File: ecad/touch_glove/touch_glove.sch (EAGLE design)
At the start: 374 parts, among them IC1 DRV8662, J1 VERT MALE 2.54MM, J2 VERT MALE 2.54MM, J3 VERT MALE 2.54MM, J4 VERT MALE 2.54MM, J5 VERT MALE 2.54MM, J6 PTH VERT MALE, J7 PTH VERT MALE, J8 PTH VERT MALE, J9 PTH VERT MALE, Q1 MCH3474 4A/30V, Q2 MCH3474 4A/30V, Q3 MCH3474 4A/30V, Q4 MCH3474 4A/30V, Q5 MCH3474 4A/30V, Q6 MCH3474 4A/30V, SW1 4A/28V, SW2 25mA/24V

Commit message: Create mcu to unity example code.  Create schematics for master thesis.  Edit robotic arm and touch glove pcb.
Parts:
- removed JP2: JUMPER_SMD_2-PAD_NO_SILK, _connectors:JUMPER_SMD_2-PAD_NO_SILK
- AVR_ISP: value PTH VERT MALE -> AVR ISP
- FTDI: value FTDI -> PTH RA VERT MALE; device _connectors:FTDI_PTH_RA-MALE -> _connectors:FTDI_PTH_RA_MALE_2.54MM
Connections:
- removed net AREF: JP2.2, MCU.AREF
- net A1.8V: now also MCU.AREF
- net VSENSOR: no longer JP2.1
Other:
- moved on the sheet: FTDI
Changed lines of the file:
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@@
 <setting verticaltext="up"/>
 </settings>
-<grid distance="0.1" unitdist="inch" unit="inch" style="lines" multiple="1" display="yes" altdistance="0.01" altunitdist="inch" altunit="inch"/>
+<grid distance="0.1" unitdist="inch" unit="inch" style="lines" multiple="1" display="no" altdistance="0.01" altunitdist="inch" altunit="inch"/>
 <layers>
 <layer number="1" name="Top" color="4" fill="1" visible="no" active="no"/>
@@
 <part name="GND125" library="_power_symbols" deviceset="GND" device=""/>
 <part name="SUPPLY84" library="_power_symbols" deviceset="VCC" device=""/>
-<part name="AVR_ISP" library="_connectors" deviceset="AVR_SPI_PRG_6" device="_PTH_VERT_MALE_2.54MM" package3d_urn="urn:adsk.eagle:package:4860635/1" value="PTH VERT MALE"/>
+<part name="AVR_ISP" library="_connectors" deviceset="AVR_SPI_PRG_6" device="_PTH_VERT_MALE_2.54MM" package3d_urn="urn:adsk.eagle:package:8712796/1" value="AVR ISP"/>
 <part name="C22" library="_capacitors" deviceset="0.1UF" device="_SMD-0402_50V-10%" package3d_urn="urn:adsk.eagle:package:2886515/1" value="0.1uF/50V"/>
-<part name="FTDI" library="_connectors" deviceset="FTDI" device="_PTH_RA-MALE" package3d_urn="urn:adsk.eagle:package:2993075/7" value="FTDI"/>
+<part name="FTDI" library="_connectors" deviceset="FTDI" device="_PTH_RA_MALE_2.54MM" package3d_urn="urn:adsk.eagle:package:8712641/1" value="PTH RA VERT MALE"/>
 <part name="GND127" library="_power_symbols" deviceset="GND" device=""/>
 <part name="GND128" library="_power_symbols" deviceset="GND" device=""/>
@@
 <part name="SUPPLY3" library="_power_symbols" deviceset="NGND" device=""/>
 <part name="SUPPLY6" library="_power_symbols" deviceset="NGND" device=""/>
-<part name="SW1" library="_switches" library_urn="urn:adsk.eagle:library:8465428" deviceset="SWITCH_SPDT" device="_RA_PTH_4A-28V_L12.7-W9.5" package3d_urn="urn:adsk.eagle:package:2973750/5" value="4A/28V"/>
+<part name="SW1" library="_switches" deviceset="SWITCH_SPDT" device="_RA_PTH_4A-28V_L12.7-W9.5" package3d_urn="urn:adsk.eagle:package:2973750/2" value="4A/28V"/>
 <part name="C1" library="_capacitors" deviceset="100UF-POLARIZED" device="_TANT_SMD-1206_10V-20%" package3d_urn="urn:adsk.eagle:package:6906990/1" value="100uF/10V"/>
 <part name="SUPPLY4" library="_power_symbols" deviceset="GND" device=""/>
@@
 <part name="SUPPLY120" library="_power_symbols" deviceset="VSENSOR" device=""/>
 <part name="SUPPLY121" library="_power_symbols" deviceset="VSENSOR" device=""/>
-<part name="JP2" library="_connectors" deviceset="JUMPER_SMD_2-PAD_NO" device="_SILK"/>
-<part name="SUPPLY13" library="_power_symbols" deviceset="VSENSOR" device=""/>
 <part name="SUPPLY15" library="_power_symbols" deviceset="VBAT" device=""/>
 <part name="OPAMP1" library="_op_amps" deviceset="LM358" device="_DFN-EP" package3d_urn="urn:adsk.eagle:package:2992818/3" value="LM358"/>
@@
 <part name="J9" library="_connectors" deviceset="1X02" device="_PTH_VERT_MALE_2.54MM" package3d_urn="urn:adsk.eagle:package:4781708/8" value="PTH VERT MALE"/>
 <part name="SUPPLY51" library="_power_symbols" deviceset="NGND" device=""/>
+<part name="SUPPLY52" library="_power_symbols" deviceset="A1.8V" device=""/>
 </parts>
 <sheets>
@@
 <instance part="SUPPLY120" gate="G$1" x="436.88" y="436.88" smashed="yes"/>
 <instance part="SUPPLY121" gate="G$1" x="447.04" y="436.88" smashed="yes"/>
-<instance part="JP2" gate="G$1" x="297.18" y="411.48" smashed="yes">
-<attribute name="NAME" x="297.18" y="413.258" size="1.27" layer="95" font="vector" ratio="10" align="bottom-center"/>
-</instance>
-<instance part="SUPPLY13" gate="G$1" x="289.56" y="419.1" smashed="yes"/>
 <instance part="SUPPLY15" gate="G$1" x="274.32" y="274.32" smashed="yes"/>
 <instance part="OPAMP1" gate="G$1" x="548.64" y="330.2" smashed="yes">
@@
 </instance>
 <instance part="SUPPLY51" gate="G$1" x="662.94" y="454.66" smashed="yes"/>
+<instance part="SUPPLY52" gate="G$1" x="299.72" y="419.1" smashed="yes"/>
 </instances>
 <busses>
@@
 <segment>
 <pinref part="FTDI" gate="G$1" pin="GND"/>
-<wire x1="246.38" y1="91.44" x2="248.92" y2="91.44" width="0.1524" layer="91"/>
+<wire x1="243.84" y1="91.44" x2="248.92" y2="91.44" width="0.1524" layer="91"/>
 <wire x1="248.92" y1="91.44" x2="248.92" y2="88.9" width="0.1524" layer="91"/>
 <pinref part="GND127" gate="GND" pin="GND"/>
@@
 <segment>
 <pinref part="FTDI" gate="G$1" pin="TXO"/>
-<wire x1="251.46" y1="96.52" x2="246.38" y2="96.52" width="0.1524" layer="91"/>
+<wire x1="251.46" y1="96.52" x2="243.84" y2="96.52" width="0.1524" layer="91"/>
 <label x="251.46" y="96.52" size="1.27" layer="95" font="vector" ratio="10" xref="yes"/>
 </segment>
@@
 <segment>
 <pinref part="FTDI" gate="G$1" pin="RXI"/>
-<wire x1="246.38" y1="99.06" x2="251.46" y2="99.06" width="0.1524" layer="91"/>
+<wire x1="243.84" y1="99.06" x2="251.46" y2="99.06" width="0.1524" layer="91"/>
 <label x="251.46" y="99.06" size="1.27" layer="95" font="vector" ratio="10" xref="yes"/>
 </segment>
@@
 <pinref part="FTDI" gate="G$1" pin="DTR"/>
 <pinref part="C22" gate="G$1" pin="1"/>
-<wire x1="259.08" y1="101.6" x2="246.38" y2="101.6" width="0.1524" layer="91"/>
+<wire x1="259.08" y1="101.6" x2="243.84" y2="101.6" width="0.1524" layer="91"/>
 </segment>
 </net>
@@
 </segment>
 <segment>
-<pinref part="SUPPLY13" gate="G$1" pin="VSENSOR"/>
-<wire x1="289.56" y1="419.1" x2="289.56" y2="411.48" width="0.1524" layer="91" style="longdash"/>
-<pinref part="JP2" gate="G$1" pin="1"/>
-<wire x1="289.56" y1="411.48" x2="292.1" y2="411.48" width="0.1524" layer="91" style="longdash"/>
-</segment>
-<segment>
 <pinref part="OPAMP1" gate="G$1" pin="V+"/>
 <wire x1="548.64" y1="345.44" x2="548.64" y2="342.9" width="0.1524" layer="91"/>
@@
 </segment>
 </net>
-<net name="AREF" class="0">
-<segment>
-<pinref part="JP2" gate="G$1" pin="2"/>
-<pinref part="MCU" gate="G$1" pin="AREF"/>
-<wire x1="302.26" y1="411.48" x2="304.8" y2="411.48" width="0.1524" layer="91" style="longdash"/>
-</segment>
-</net>
 <net name="S1" class="0">
 <segment>
@@
 <wire x1="279.4" y1="190.5" x2="279.4" y2="187.96" width="0.1524" layer="91"/>
 </segment>
+<segment>
+<pinref part="MCU" gate="G$1" pin="AREF"/>
+<wire x1="299.72" y1="411.48" x2="304.8" y2="411.48" width="0.1524" layer="91" style="longdash"/>
+<wire x1="299.72" y1="411.48" x2="299.72" y2="419.1" width="0.1524" layer="91"/>
+<pinref part="SUPPLY52" gate="G$1" pin="A1.8V"/>
+</segment>
 </net>
 <net name="INDEX_IN1-4" class="0">
@@
 </drawing>
 <compatibility>
-<note version="8.2" severity="warning">
-Since Version 8.2, EAGLE supports online libraries. The ids
-of those online libraries will not be understood (or retained)
-with this version.
+<note version="6.3" minversion="6.2.2" severity="warning">
+Since Version 6.2.2 text objects can contain more than one line,
+which will not be processed correctly with this version.
 </note>
 <note version="8.3" severity="warning">

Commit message: Create PCA9685Servo library.  Touch up Touch Glove PCB.  Major work completed on ET Extension.
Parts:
- removed C16, C19, C37, C49, C63, C64, C66, C67, C68, C69, C70, C76, C78, C80: 0.1uF/50V, _capacitors:0.1UF_SMD-0402_50V-10%
- removed C17, C20, C71, C72, C73, C75, C77, C79: 10uF/6.3V, _capacitors:10UF_CER_SMD-0402_6.3V-20%
- removed C61: 0.1uF/25V, _capacitors:0.1UF_SMD-0603_50V-20%
- removed C62: 0.1uF/250V, _capacitors:0.1UF_SMD-0805_250V-10%
- removed C65: 100uF/10V, _capacitors:100UF-POLARIZED_TANT_SMD-1206_10V-20%
- removed C74: 4.7uF/10V/0402, _capacitors:4.7UF_CER_SMD-0402_10V-20%
- removed ET_INDEX_PIXEL1-1, ET_INDEX_PIXEL1-10, ET_INDEX_PIXEL1-11, ET_INDEX_PIXEL1-12, ET_INDEX_PIXEL1-13, ET_INDEX_PIXEL1-14, ET_INDEX_PIXEL1-15, ET_INDEX_PIXEL1-16, ET_INDEX_PIXEL1-17, ET_INDEX_PIXEL1-18, ET_INDEX_PIXEL1-19, ET_INDEX_PIXEL1-2, ET_INDEX_PIXEL1-20, ET_INDEX_PIXEL1-3, ET_INDEX_PIXEL1-4, ET_INDEX_PIXEL1-5, ET_INDEX_PIXEL1-6, ET_INDEX_PIXEL1-7, ET_INDEX_PIXEL1-8, ET_INDEX_PIXEL1-9, ET_INDEX_PIXEL2-1, ET_INDEX_PIXEL2-10, ET_INDEX_PIXEL2-11, ET_INDEX_PIXEL2-12, ET_INDEX_PIXEL2-13, ET_INDEX_PIXEL2-14, ET_INDEX_PIXEL2-15, ET_INDEX_PIXEL2-16, ET_INDEX_PIXEL2-17, ET_INDEX_PIXEL2-18, ET_INDEX_PIXEL2-19, ET_INDEX_PIXEL2-2, ET_INDEX_PIXEL2-20, ET_INDEX_PIXEL2-3, ET_INDEX_PIXEL2-4, ET_INDEX_PIXEL2-5, ET_INDEX_PIXEL2-6, ET_INDEX_PIXEL2-7, ET_INDEX_PIXEL2-8, ET_INDEX_PIXEL2-9, ET_INDEX_PIXEL3-1, ET_INDEX_PIXEL3-10, ET_INDEX_PIXEL3-11, ET_INDEX_PIXEL3-12, ET_INDEX_PIXEL3-13, ET_INDEX_PIXEL3-14, ET_INDEX_PIXEL3-15, ET_INDEX_PIXEL3-16, ET_INDEX_PIXEL3-17, ET_INDEX_PIXEL3-18, ET_INDEX_PIXEL3-19, ET_INDEX_PIXEL3-2, ET_INDEX_PIXEL3-20, ET_INDEX_PIXEL3-3, ET_INDEX_PIXEL3-4, ET_INDEX_PIXEL3-5, ET_INDEX_PIXEL3-6, ET_INDEX_PIXEL3-7, ET_INDEX_PIXEL3-8, ET_INDEX_PIXEL3-9, ET_INDEX_PIXEL4-1, ET_INDEX_PIXEL4-10, ET_INDEX_PIXEL4-11, ET_INDEX_PIXEL4-12, ET_INDEX_PIXEL4-13, ET_INDEX_PIXEL4-14, ET_INDEX_PIXEL4-15, ET_INDEX_PIXEL4-16, ET_INDEX_PIXEL4-17, ET_INDEX_PIXEL4-18, ET_INDEX_PIXEL4-19, ET_INDEX_PIXEL4-2, ET_INDEX_PIXEL4-20, ET_INDEX_PIXEL4-3, ET_INDEX_PIXEL4-4, ET_INDEX_PIXEL4-5, ET_INDEX_PIXEL4-6, ET_INDEX_PIXEL4-7, ET_INDEX_PIXEL4-8, ET_INDEX_PIXEL4-9: SPST-NO 170mA 250V, _relay:RELAY_SOLID-STATE_SSR_170MA_250V_SPST-NO
- removed IC1: DRV8662, _special:DRV8662_PIEZO_HAPTICS_DRIVER_QFN-20-EP
- removed J1, J2, J3, J4, J5: VERT MALE 2.54MM, _connectors:1X16_PTH_VERT_MALE_2.54MM
- removed L3: 4.7uH/1.4A, _inductors:4.7UH_SMD-2520_1.4A-0.216OHM-20%
- removed L4: 10uH/380mA, _inductors:10UH_SMD-0603_0.38A-0.468OHM-10%
- removed NFET1: 2N7002DW, _transistors:MOSFET_N-CHANNEL_2-ARRAY_2N7002DW_115MA-60V
- removed OPAMP4: TLV2361_GP_20MA_7MHZ, _op_amps:TLV2361_GP_20MA_7MHZ
- removed POT1: 100K, _resistors:POTENTIOMETER_ST4ETB104_100K-1/4W-20%
- removed PWM_DRIVER2, PWM_DRIVER3, PWM_DRIVER4, PWM_DRIVER5, PWM_DRIVER6: PCA9685, _special:PCA9685_16-CH_12-BIT_PWM-DRIVER_TSSOP-28_PWM-DRIVER_16CH
- removed R100, R101, R102, R103, R104, R105, R106, R107, R108, R109, R110, R111, R112, R113, R114, R115, R116, R117, R118, R119, R120, R121, R122, R123, R124, R125, R126, R127, R128, R129, R130, R131, R132, R133, R134, R135, R49, R57, R58, R59, R60, R61, R62, R63, R64, R65, R66, R67, R68, R69, R70, R71, R72, R73, R74, R75, R76, R77, R78, R79, R80, R81, R82, R83, R84, R85, R86, R87, R88, R89, R90, R91, R92, R93, R94, R95, R96, R97, R98, R99: 1K, _resistors:1KΩ_SMD-0402_1/16W-5%
- removed R136, R137, R54, R55, R56: 10K, _resistors:10KΩ_SMD-0402_1/16W-5%
- removed R16, R17, R18, R19, R20, R21, R22, R23, R24, R25, R26, R27, R28, R29, R30, R31: 100, _resistors:100Ω_SMD-0402_1/16W-5%
- removed R50: 768K, _resistors:768KΩ_SMD-0402_1/16W-1%
- removed R51: 35.7K, _resistors:35.7KΩ_SMD-0402_1/16W-1%
- removed R52: 20K, _resistors:20KΩ_SMD-0402_1/16W-1%
- removed R53: 41.2K, _resistors:41.2KΩ_SMD-0402_1/16W-1%
- removed REXT: 7.5K, _resistors:7.5KΩ_SMD-0402_1/16W-1%
- removed SW2: 25mA/24V, _switches:SWITCH_SPST_ARRAY-3_SLIDE_DIP_SPST_25MA_24V
- removed VREG-MCU1: TPS76833QDR 1A/3.3V, _ic_power:VREG_TPS768XX_ULDO_FAST-TRANSIENT_TPS76833QDR_1A-3.3V
- removed VREG2: NCP1729 50mA, _ic_power:VREG_NCP1729_NEGATIVE_SWITCHED-CAP-INVERTER_50MA
- removed VREG3: TPS62202 300mA 1.8V, _ic_power:VREG_SWITCHING_TPS6220XTPS62202_300MA_1.8V
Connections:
- net AVCC renamed A3.3V
- removed net -1.8V: C72.1, OPAMP4.V-, VREG2.VOUT
- removed net C+: C71.1, VREG2.C+
- removed net C-: C71.2, VREG2.C-
- removed net EN: IC1.EN, R54.2, SW2.S3
- removed net FB: IC1.FB, R50.1, R51.2, R52.2, R53.2
- removed net GAIN0: IC1.GAIN0, NFET1.G2, R55.2, SW2.S2
- removed net GAIN1: IC1.GAIN1, NFET1.G1, R56.2, SW2.S1
- removed net IN+: C64.1, OPAMP4.OUT, POT1.CCW, POT1.S, R136.2
- removed net INDEX_IN1-1: ET_INDEX_PIXEL1-1.1, ET_INDEX_PIXEL1-13.1, ET_INDEX_PIXEL1-17.1, ET_INDEX_PIXEL1-5.1, ET_INDEX_PIXEL1-9.1, PWM_DRIVER2.PWM0, PWM_DRIVER3.PWM0, PWM_DRIVER4.PWM0, PWM_DRIVER5.PWM0, PWM_DRIVER6.PWM0
- removed net INDEX_IN1-2: ET_INDEX_PIXEL1-10.1, ET_INDEX_PIXEL1-14.1, ET_INDEX_PIXEL1-18.1, ET_INDEX_PIXEL1-2.1, ET_INDEX_PIXEL1-6.1, PWM_DRIVER2.PWM1, PWM_DRIVER3.PWM1, PWM_DRIVER4.PWM1, PWM_DRIVER5.PWM1, PWM_DRIVER6.PWM1
- removed net INDEX_IN1-3: ET_INDEX_PIXEL1-11.1, ET_INDEX_PIXEL1-15.1, ET_INDEX_PIXEL1-19.1, ET_INDEX_PIXEL1-3.1, ET_INDEX_PIXEL1-7.1, PWM_DRIVER2.PWM2, PWM_DRIVER3.PWM2, PWM_DRIVER4.PWM2, PWM_DRIVER5.PWM2, PWM_DRIVER6.PWM2
- removed net INDEX_IN1-4: ET_INDEX_PIXEL1-12.1, ET_INDEX_PIXEL1-16.1, ET_INDEX_PIXEL1-20.1, ET_INDEX_PIXEL1-4.1, ET_INDEX_PIXEL1-8.1, PWM_DRIVER2.PWM3, PWM_DRIVER3.PWM3, PWM_DRIVER4.PWM3, PWM_DRIVER5.PWM3, PWM_DRIVER6.PWM3
- removed net INDEX_IN2-1: ET_INDEX_PIXEL2-1.1, ET_INDEX_PIXEL2-11.1, ET_INDEX_PIXEL2-15.1, ET_INDEX_PIXEL2-19.1, ET_INDEX_PIXEL2-7.1, PWM_DRIVER2.PWM4, PWM_DRIVER3.PWM4, PWM_DRIVER4.PWM4, PWM_DRIVER5.PWM4, PWM_DRIVER6.PWM4
- removed net INDEX_IN2-2: ET_INDEX_PIXEL2-10.1, ET_INDEX_PIXEL2-14.1, ET_INDEX_PIXEL2-18.1, ET_INDEX_PIXEL2-2.1, ET_INDEX_PIXEL2-6.1, PWM_DRIVER2.PWM5, PWM_DRIVER3.PWM5, PWM_DRIVER4.PWM5, PWM_DRIVER5.PWM5, PWM_DRIVER6.PWM5
- removed net INDEX_IN2-3: ET_INDEX_PIXEL2-13.1, ET_INDEX_PIXEL2-17.1, ET_INDEX_PIXEL2-3.1, ET_INDEX_PIXEL2-5.1, ET_INDEX_PIXEL2-9.1, PWM_DRIVER2.PWM6, PWM_DRIVER3.PWM6, PWM_DRIVER4.PWM6, PWM_DRIVER5.PWM6, PWM_DRIVER6.PWM6
- removed net INDEX_IN2-4: ET_INDEX_PIXEL2-12.1, ET_INDEX_PIXEL2-16.1, ET_INDEX_PIXEL2-20.1, ET_INDEX_PIXEL2-4.1, ET_INDEX_PIXEL2-8.1, PWM_DRIVER2.PWM7, PWM_DRIVER3.PWM7, PWM_DRIVER4.PWM7, PWM_DRIVER5.PWM7, PWM_DRIVER6.PWM7
- removed net INDEX_IN3-1: ET_INDEX_PIXEL3-1.1, ET_INDEX_PIXEL3-13.1, ET_INDEX_PIXEL3-17.1, ET_INDEX_PIXEL3-5.1, ET_INDEX_PIXEL3-9.1, PWM_DRIVER2.PWM8, PWM_DRIVER3.PWM8, PWM_DRIVER4.PWM8, PWM_DRIVER5.PWM8, PWM_DRIVER6.PWM8
- removed net INDEX_IN3-2: ET_INDEX_PIXEL3-10.1, ET_INDEX_PIXEL3-14.1, ET_INDEX_PIXEL3-18.1, ET_INDEX_PIXEL3-2.1, ET_INDEX_PIXEL3-6.1, PWM_DRIVER2.PWM9, PWM_DRIVER3.PWM9, PWM_DRIVER4.PWM9, PWM_DRIVER5.PWM9, PWM_DRIVER6.PWM9
- removed net INDEX_IN3-3: ET_INDEX_PIXEL3-11.1, ET_INDEX_PIXEL3-15.1, ET_INDEX_PIXEL3-19.1, ET_INDEX_PIXEL3-3.1, ET_INDEX_PIXEL3-7.1, PWM_DRIVER2.PWM10, PWM_DRIVER3.PWM10, PWM_DRIVER4.PWM10, PWM_DRIVER5.PWM10, PWM_DRIVER6.PWM10
- removed net INDEX_IN3-4: ET_INDEX_PIXEL3-12.1, ET_INDEX_PIXEL3-16.1, ET_INDEX_PIXEL3-20.1, ET_INDEX_PIXEL3-4.1, ET_INDEX_PIXEL3-8.1, PWM_DRIVER2.PWM11, PWM_DRIVER3.PWM11, PWM_DRIVER4.PWM11, PWM_DRIVER5.PWM11, PWM_DRIVER6.PWM11
- removed net INDEX_IN4-1: ET_INDEX_PIXEL4-1.1, ET_INDEX_PIXEL4-13.1, ET_INDEX_PIXEL4-17.1, ET_INDEX_PIXEL4-5.1, ET_INDEX_PIXEL4-9.1, PWM_DRIVER2.PWM12, PWM_DRIVER3.PWM12, PWM_DRIVER4.PWM12, PWM_DRIVER5.PWM12, PWM_DRIVER6.PWM12
- removed net INDEX_IN4-2: ET_INDEX_PIXEL4-10.1, ET_INDEX_PIXEL4-14.1, ET_INDEX_PIXEL4-18.1, ET_INDEX_PIXEL4-2.1, ET_INDEX_PIXEL4-6.1, PWM_DRIVER2.PWM13, PWM_DRIVER3.PWM13, PWM_DRIVER4.PWM13, PWM_DRIVER5.PWM13, PWM_DRIVER6.PWM13
- removed net INDEX_IN4-3: ET_INDEX_PIXEL4-11.1, ET_INDEX_PIXEL4-15.1, ET_INDEX_PIXEL4-19.1, ET_INDEX_PIXEL4-3.1, ET_INDEX_PIXEL4-7.1, PWM_DRIVER2.PWM14, PWM_DRIVER3.PWM14, PWM_DRIVER4.PWM14, PWM_DRIVER5.PWM14, PWM_DRIVER6.PWM14
- removed net INDEX_IN4-4: ET_INDEX_PIXEL4-12.1, ET_INDEX_PIXEL4-16.1, ET_INDEX_PIXEL4-20.1, ET_INDEX_PIXEL4-4.1, ET_INDEX_PIXEL4-8.1, PWM_DRIVER2.PWM15, PWM_DRIVER3.PWM15, PWM_DRIVER4.PWM15, PWM_DRIVER5.PWM15, PWM_DRIVER6.PWM15
- removed net INDEX_OUT1-1: ET_INDEX_PIXEL1-1.3, ET_INDEX_PIXEL1-13.3, ET_INDEX_PIXEL1-17.3, ET_INDEX_PIXEL1-5.3, ET_INDEX_PIXEL1-9.3, J1.1, J2.1, J3.1, J4.1, J5.1
- removed net INDEX_OUT1-2: ET_INDEX_PIXEL1-10.3, ET_INDEX_PIXEL1-14.3, ET_INDEX_PIXEL1-18.3, ET_INDEX_PIXEL1-2.3, ET_INDEX_PIXEL1-6.3
- removed net INDEX_OUT1-3: ET_INDEX_PIXEL1-11.3, ET_INDEX_PIXEL1-15.3, ET_INDEX_PIXEL1-19.3, ET_INDEX_PIXEL1-3.3, ET_INDEX_PIXEL1-7.3
- removed net INDEX_OUT1-4: ET_INDEX_PIXEL1-12.3, ET_INDEX_PIXEL1-16.3, ET_INDEX_PIXEL1-20.3, ET_INDEX_PIXEL1-4.3, ET_INDEX_PIXEL1-8.3
- removed net INDEX_OUT2-1: ET_INDEX_PIXEL2-1.3, ET_INDEX_PIXEL2-11.3, ET_INDEX_PIXEL2-15.3, ET_INDEX_PIXEL2-19.3, ET_INDEX_PIXEL2-7.3
- removed net INDEX_OUT2-2: ET_INDEX_PIXEL2-10.3, ET_INDEX_PIXEL2-14.3, ET_INDEX_PIXEL2-18.3, ET_INDEX_PIXEL2-2.3, ET_INDEX_PIXEL2-6.3
- removed net INDEX_OUT2-3: ET_INDEX_PIXEL2-13.3, ET_INDEX_PIXEL2-17.3, ET_INDEX_PIXEL2-3.3, ET_INDEX_PIXEL2-5.3, ET_INDEX_PIXEL2-9.3
- removed net INDEX_OUT2-4: ET_INDEX_PIXEL2-12.3, ET_INDEX_PIXEL2-16.3, ET_INDEX_PIXEL2-20.3, ET_INDEX_PIXEL2-4.3, ET_INDEX_PIXEL2-8.3
- removed net INDEX_OUT3-1: ET_INDEX_PIXEL3-1.3, ET_INDEX_PIXEL3-13.3, ET_INDEX_PIXEL3-17.3, ET_INDEX_PIXEL3-5.3, ET_INDEX_PIXEL3-9.3
- removed net INDEX_OUT3-2: ET_INDEX_PIXEL3-10.3, ET_INDEX_PIXEL3-14.3, ET_INDEX_PIXEL3-18.3, ET_INDEX_PIXEL3-2.3, ET_INDEX_PIXEL3-6.3
- removed net INDEX_OUT3-3: ET_INDEX_PIXEL3-11.3, ET_INDEX_PIXEL3-15.3, ET_INDEX_PIXEL3-19.3, ET_INDEX_PIXEL3-3.3, ET_INDEX_PIXEL3-7.3
- removed net INDEX_OUT3-4: ET_INDEX_PIXEL3-12.3, ET_INDEX_PIXEL3-16.3, ET_INDEX_PIXEL3-20.3, ET_INDEX_PIXEL3-4.3, ET_INDEX_PIXEL3-8.3
- removed net INDEX_OUT4-1: ET_INDEX_PIXEL4-1.3, ET_INDEX_PIXEL4-13.3, ET_INDEX_PIXEL4-17.3, ET_INDEX_PIXEL4-5.3, ET_INDEX_PIXEL4-9.3
- removed net INDEX_OUT4-2: ET_INDEX_PIXEL4-10.3, ET_INDEX_PIXEL4-14.3, ET_INDEX_PIXEL4-18.3, ET_INDEX_PIXEL4-2.3, ET_INDEX_PIXEL4-6.3
- removed net INDEX_OUT4-3: ET_INDEX_PIXEL4-11.3, ET_INDEX_PIXEL4-15.3, ET_INDEX_PIXEL4-19.3, ET_INDEX_PIXEL4-3.3, ET_INDEX_PIXEL4-7.3
- removed net INDEX_OUT4-4: ET_INDEX_PIXEL4-12.3, ET_INDEX_PIXEL4-16.3, ET_INDEX_PIXEL4-20.3, ET_INDEX_PIXEL4-4.3, ET_INDEX_PIXEL4-8.3
- removed net N$10: HBRIDGE-INDEX.IN1/PH, R24.2, R40.2
- removed net N$100: ET_INDEX_PIXEL3-12.2, R99.2
- removed net N$101: ET_INDEX_PIXEL4-9.2, R100.2
- removed net N$102: ET_INDEX_PIXEL4-10.2, R101.2
- removed net N$103: ET_INDEX_PIXEL4-11.2, R102.2
- removed net N$104: ET_INDEX_PIXEL4-12.2, R103.2
- removed net N$105: ET_INDEX_PIXEL1-13.2, R104.2
- removed net N$106: ET_INDEX_PIXEL1-14.2, R105.2
- removed net N$107: ET_INDEX_PIXEL1-15.2, R106.2
- removed net N$108: ET_INDEX_PIXEL1-16.2, R107.2
- removed net N$109: ET_INDEX_PIXEL2-15.2, R108.2
- removed net N$110: ET_INDEX_PIXEL2-14.2, R109.2
- removed net N$111: ET_INDEX_PIXEL2-13.2, R110.2
- removed net N$112: ET_INDEX_PIXEL2-16.2, R111.2
- removed net N$113: ET_INDEX_PIXEL3-13.2, R112.2
- removed net N$114: ET_INDEX_PIXEL3-14.2, R113.2
- removed net N$115: ET_INDEX_PIXEL3-15.2, R114.2
- removed net N$116: ET_INDEX_PIXEL3-16.2, R115.2
- removed net N$117: ET_INDEX_PIXEL4-13.2, R116.2
- removed net N$118: ET_INDEX_PIXEL4-14.2, R117.2
- removed net N$119: ET_INDEX_PIXEL4-15.2, R118.2
- removed net N$120: ET_INDEX_PIXEL4-16.2, R119.2
- removed net N$121: ET_INDEX_PIXEL1-17.2, R120.2
- removed net N$122: ET_INDEX_PIXEL1-18.2, R121.2
- removed net N$123: ET_INDEX_PIXEL1-19.2, R122.2
- removed net N$124: ET_INDEX_PIXEL1-20.2, R123.2
- removed net N$125: ET_INDEX_PIXEL2-19.2, R124.2
- removed net N$126: ET_INDEX_PIXEL2-18.2, R125.2
- removed net N$127: ET_INDEX_PIXEL2-17.2, R126.2
- removed net N$128: ET_INDEX_PIXEL2-20.2, R127.2
- removed net N$129: ET_INDEX_PIXEL3-17.2, R128.2
- removed net N$13: HBRIDGE-MIDDLE.IN2/EN, R27.2, R43.2
- removed net N$130: ET_INDEX_PIXEL3-18.2, R129.2
- removed net N$131: ET_INDEX_PIXEL3-19.2, R130.2
- removed net N$132: ET_INDEX_PIXEL3-20.2, R131.2
- removed net N$133: ET_INDEX_PIXEL4-17.2, R132.2
- removed net N$134: ET_INDEX_PIXEL4-18.2, R133.2
- removed net N$135: ET_INDEX_PIXEL4-19.2, R134.2
- removed net N$136: ET_INDEX_PIXEL4-20.2, R135.2
- removed net N$137: L4.1, VREG3.VOUT
- removed net N$138: OPAMP4.IN+, R136.1, R137.2
- removed net N$139: C76.1, OPAMP4.IN-, POT1.CW
- removed net N$14: HBRIDGE-MIDDLE.IN1/PH, R26.2, R42.2
- removed net N$19: HBRIDGE-RING.IN2/EN, R29.2, R45.2
- removed net N$20: HBRIDGE-RING.IN1/PH, R28.2, R44.2
- removed net N$21: Q4.G, R19.2, R35.2
- removed net N$22: Q5.G, R20.2, R36.2
- removed net N$25: HBRIDGE-PINKY.IN2/EN, R31.2, R47.2
- removed net N$26: HBRIDGE-PINKY.IN1/PH, R30.2, R46.2
- removed net N$28: Q1.G, R16.2, R32.2
- removed net N$29: HBRIDGE-THUMB.IN2/EN, R23.2, R39.2
- removed net N$31: HBRIDGE-THUMB.IN1/PH, R22.2, R38.2
- removed net N$32: Q6.G, R21.2, R37.2
- removed net N$33: ET_INDEX_PIXEL1-3.2, R58.2
- removed net N$39: ET_INDEX_PIXEL1-1.2, R49.2
- removed net N$42: IC1.SW, L3.1
- removed net N$43: C49.1, IC1.VPUMP
- removed net N$44: C62.1, IC1.PVDD, IC1.VBST, R50.2
- removed net N$48: IC1.REXT, REXT.2
- removed net N$49: NFET1.D1, R52.1
- removed net N$51: NFET1.D2, R53.1
- removed net N$52: C64.2, IC1.IN+
- removed net N$56: C63.2, IC1.IN-
- removed net N$57: ET_INDEX_PIXEL1-2.2, R57.2
- removed net N$58: ET_INDEX_PIXEL1-5.2, R72.2
- removed net N$59: ET_INDEX_PIXEL1-4.2, R59.2
- removed net N$60: ET_INDEX_PIXEL2-1.2, R60.2
- removed net N$61: ET_INDEX_PIXEL2-2.2, R61.2
- removed net N$64: ET_INDEX_PIXEL2-3.2, R62.2
- removed net N$65: ET_INDEX_PIXEL2-4.2, R63.2
- removed net N$66: ET_INDEX_PIXEL3-1.2, R64.2
- removed net N$67: ET_INDEX_PIXEL3-2.2, R65.2
- removed net N$68: ET_INDEX_PIXEL3-3.2, R66.2
- removed net N$69: ET_INDEX_PIXEL3-4.2, R67.2
- removed net N$7: Q2.G, R17.2, R33.2, VREG3.EN
- removed net N$70: ET_INDEX_PIXEL4-1.2, R68.2
- removed net N$71: ET_INDEX_PIXEL4-2.2, R69.2
- removed net N$72: ET_INDEX_PIXEL4-3.2, R70.2
- removed net N$73: ET_INDEX_PIXEL4-4.2, R71.2
- removed net N$74: ET_INDEX_PIXEL1-6.2, R73.2
- removed net N$75: ET_INDEX_PIXEL1-7.2, R74.2
- removed net N$76: ET_INDEX_PIXEL1-8.2, R75.2
- removed net N$77: ET_INDEX_PIXEL2-7.2, R76.2
- removed net N$78: ET_INDEX_PIXEL2-6.2, R77.2
- removed net N$79: ET_INDEX_PIXEL2-5.2, R78.2
- removed net N$8: HBRIDGE-INDEX.IN2/EN, R25.2, R41.2
- removed net N$80: ET_INDEX_PIXEL2-8.2, R79.2
- removed net N$81: ET_INDEX_PIXEL3-5.2, R80.2
- removed net N$82: ET_INDEX_PIXEL3-6.2, R81.2
- removed net N$83: ET_INDEX_PIXEL3-7.2, R82.2
- removed net N$84: ET_INDEX_PIXEL3-8.2, R83.2
- removed net N$85: ET_INDEX_PIXEL4-5.2, R84.2
- removed net N$86: ET_INDEX_PIXEL4-6.2, R85.2
- removed net N$87: ET_INDEX_PIXEL4-7.2, R86.2
- removed net N$88: ET_INDEX_PIXEL4-8.2, R87.2
- removed net N$89: ET_INDEX_PIXEL1-9.2, R88.2
- removed net N$9: Q3.G, R18.2, R34.2
- removed net N$90: ET_INDEX_PIXEL1-10.2, R89.2
- removed net N$91: ET_INDEX_PIXEL1-11.2, R90.2
- removed net N$92: ET_INDEX_PIXEL1-12.2, R91.2
- removed net N$93: ET_INDEX_PIXEL2-11.2, R92.2
- removed net N$94: ET_INDEX_PIXEL2-10.2, R93.2
- removed net N$95: ET_INDEX_PIXEL2-9.2, R94.2
- removed net N$96: ET_INDEX_PIXEL2-12.2, R95.2
- removed net N$97: ET_INDEX_PIXEL3-9.2, R96.2
- removed net N$98: ET_INDEX_PIXEL3-10.2, R97.2
- removed net N$99: ET_INDEX_PIXEL3-11.2, R98.2
- removed net V+: ET_INDEX_PIXEL1-1.4, ET_INDEX_PIXEL1-10.4, ET_INDEX_PIXEL1-11.4, ET_INDEX_PIXEL1-12.4, ET_INDEX_PIXEL1-13.4, ET_INDEX_PIXEL1-14.4, ET_INDEX_PIXEL1-15.4, ET_INDEX_PIXEL1-16.4, ET_INDEX_PIXEL1-17.4, ET_INDEX_PIXEL1-18.4, ET_INDEX_PIXEL1-19.4, ET_INDEX_PIXEL1-2.4, ET_INDEX_PIXEL1-20.4, ET_INDEX_PIXEL1-3.4, ET_INDEX_PIXEL1-4.4, ET_INDEX_PIXEL1-5.4, ET_INDEX_PIXEL1-6.4, ET_INDEX_PIXEL1-7.4, ET_INDEX_PIXEL1-8.4, ET_INDEX_PIXEL1-9.4, ET_INDEX_PIXEL2-1.4, ET_INDEX_PIXEL2-10.4, ET_INDEX_PIXEL2-11.4, ET_INDEX_PIXEL2-12.4, ET_INDEX_PIXEL2-13.4, ET_INDEX_PIXEL2-14.4, ET_INDEX_PIXEL2-15.4, ET_INDEX_PIXEL2-16.4, ET_INDEX_PIXEL2-17.4, ET_INDEX_PIXEL2-18.4, ET_INDEX_PIXEL2-19.4, ET_INDEX_PIXEL2-2.4, ET_INDEX_PIXEL2-20.4, ET_INDEX_PIXEL2-3.4, ET_INDEX_PIXEL2-4.4, ET_INDEX_PIXEL2-5.4, ET_INDEX_PIXEL2-6.4, ET_INDEX_PIXEL2-7.4, ET_INDEX_PIXEL2-8.4, ET_INDEX_PIXEL2-9.4, ET_INDEX_PIXEL3-1.4, ET_INDEX_PIXEL3-10.4, ET_INDEX_PIXEL3-11.4, ET_INDEX_PIXEL3-12.4, ET_INDEX_PIXEL3-13.4, ET_INDEX_PIXEL3-14.4, ET_INDEX_PIXEL3-15.4, ET_INDEX_PIXEL3-16.4, ET_INDEX_PIXEL3-17.4, ET_INDEX_PIXEL3-18.4, ET_INDEX_PIXEL3-19.4, ET_INDEX_PIXEL3-2.4, ET_INDEX_PIXEL3-20.4, ET_INDEX_PIXEL3-3.4, ET_INDEX_PIXEL3-4.4, ET_INDEX_PIXEL3-5.4, ET_INDEX_PIXEL3-6.4, ET_INDEX_PIXEL3-7.4, ET_INDEX_PIXEL3-8.4, ET_INDEX_PIXEL3-9.4, ET_INDEX_PIXEL4-1.4, ET_INDEX_PIXEL4-10.4, ET_INDEX_PIXEL4-11.4, ET_INDEX_PIXEL4-12.4, ET_INDEX_PIXEL4-13.4, ET_INDEX_PIXEL4-14.4, ET_INDEX_PIXEL4-15.4, ET_INDEX_PIXEL4-16.4, ET_INDEX_PIXEL4-17.4, ET_INDEX_PIXEL4-18.4, ET_INDEX_PIXEL4-19.4, ET_INDEX_PIXEL4-2.4, ET_INDEX_PIXEL4-20.4, ET_INDEX_PIXEL4-3.4, ET_INDEX_PIXEL4-4.4, ET_INDEX_PIXEL4-5.4, ET_INDEX_PIXEL4-6.4, ET_INDEX_PIXEL4-7.4, ET_INDEX_PIXEL4-8.4, ET_INDEX_PIXEL4-9.4, IC1.OUT+
- removed net V-: IC1.OUT-, J1.16, J2.16, J3.16, J4.16, J5.16
- net 1.8V: no longer C19.1, C20.1, C73.1, C75.1, L4.2, OPAMP4.V+, VREG2.!SHDN, VREG2.VIN, VREG3.NC/FB
- net 3.3V: no longer C16.1, C17.1, C37.1, C61.1, C65.A, C74.1, C77.1, C78.1, IC1.VDD, L3.2, SW2.P1, SW2.P2, SW2.P3, VREG-MCU1.VOUT, VREG3.VIN
- net GND: no longer C37.2, C49.2, C61.2, C62.2, C63.1, C65.K, C66.2, C67.2, C68.2, C69.2, C70.2, C72.2, C73.2, C74.2, C75.2, C76.2, C77.2, C78.2, C79.2, C80.2, IC1.GND, NFET1.S1, NFET1.S2, PWM_DRIVER2.!OE, PWM_DRIVER2.A0, PWM_DRIVER2.A1, PWM_DRIVER2.A2, PWM_DRIVER2.A3, PWM_DRIVER2.A4, PWM_DRIVER2.A5, PWM_DRIVER2.EXTCLK, PWM_DRIVER2.GND, PWM_DRIVER3.!OE, PWM_DRIVER3.A0, PWM_DRIVER3.A1, PWM_DRIVER3.A2, PWM_DRIVER3.A3, PWM_DRIVER3.A4, PWM_DRIVER3.A5, PWM_DRIVER3.EXTCLK, PWM_DRIVER3.GND, PWM_DRIVER4.!OE, PWM_DRIVER4.A0, PWM_DRIVER4.A1, PWM_DRIVER4.A2, PWM_DRIVER4.A3, PWM_DRIVER4.A4, PWM_DRIVER4.A5, PWM_DRIVER4.EXTCLK, PWM_DRIVER4.GND, PWM_DRIVER5.!OE, PWM_DRIVER5.A0, PWM_DRIVER5.A1, PWM_DRIVER5.A2, PWM_DRIVER5.A3, PWM_DRIVER5.A4, PWM_DRIVER5.A5, PWM_DRIVER5.EXTCLK, PWM_DRIVER5.GND, PWM_DRIVER6.!OE, PWM_DRIVER6.A0, PWM_DRIVER6.A1, PWM_DRIVER6.A2, PWM_DRIVER6.A3, PWM_DRIVER6.A4, PWM_DRIVER6.A5, PWM_DRIVER6.EXTCLK, PWM_DRIVER6.GND, R100.1, R101.1, R102.1, R103.1, R104.1, R105.1, R106.1, R107.1, R108.1, R109.1, R110.1, R111.1, R112.1, R113.1, R114.1, R115.1, R116.1, R117.1, R118.1, R119.1, R120.1, R121.1, R122.1, R123.1, R124.1, R125.1, R126.1, R127.1, R128.1, R129.1, R130.1, R131.1, R132.1, R133.1, R134.1, R135.1, R137.1, R49.1, R51.1, R54.1, R55.1, R56.1, R57.1, R58.1, R59.1, R60.1, R61.1, R62.1, R63.1, R64.1, R65.1, R66.1, R67.1, R68.1, R69.1, R70.1, R71.1, R72.1, R73.1, R74.1, R75.1, R76.1, R77.1, R78.1, R79.1, R80.1, R81.1, R82.1, R83.1, R84.1, R85.1, R86.1, R87.1, R88.1, R89.1, R90.1, R91.1, R92.1, R93.1, R94.1, R95.1, R96.1, R97.1, R98.1, R99.1, REXT.1, VREG-MCU1.!EN, VREG-MCU1.GND, VREG2.GND, VREG3.GND
- net NGND: no longer C16.2, C17.2, C19.2, C20.2
- net SCL: no longer PWM_DRIVER2.SCL, PWM_DRIVER3.SCL, PWM_DRIVER4.SCL, PWM_DRIVER5.SCL, PWM_DRIVER6.SCL
- net SDA: no longer PWM_DRIVER2.SDA, PWM_DRIVER3.SDA, PWM_DRIVER4.SDA, PWM_DRIVER5.SDA, PWM_DRIVER6.SDA
- net TEC-INDEX-COLD: now also HBRIDGE-INDEX.IN2/EN, R41.2; no longer R25.1
- net TEC-INDEX-HOT: now also HBRIDGE-INDEX.IN1/PH, R40.2; no longer R24.1
- net TEC-MIDDLE-COLD: now also HBRIDGE-MIDDLE.IN2/EN, R43.2; no longer R27.1
- net TEC-MIDDLE-HOT: now also HBRIDGE-MIDDLE.IN1/PH, R42.2; no longer R26.1
- net TEC-PINKY-COLD: now also HBRIDGE-PINKY.IN2/EN, R47.2; no longer R31.1
- net TEC-PINKY-HOT: now also HBRIDGE-PINKY.IN1/PH, R46.2; no longer R30.1
- net TEC-RING-COLD: now also HBRIDGE-RING.IN2/EN, R45.2; no longer R29.1
- net TEC-RING-HOT: now also HBRIDGE-RING.IN1/PH, R44.2; no longer R28.1
- net TEC-THUMB-COLD: now also HBRIDGE-THUMB.IN2/EN, R39.2; no longer R23.1
- net TEC-THUMB-HOT: now also HBRIDGE-THUMB.IN1/PH, R38.2; no longer R22.1
- net VBAT: no longer C79.1, C80.1, VREG-MCU1.VIN
- net VCC: no longer C66.1, C67.1, C68.1, C69.1, C70.1, PWM_DRIVER2.VCC, PWM_DRIVER3.VCC, PWM_DRIVER4.VCC, PWM_DRIVER5.VCC, PWM_DRIVER6.VCC
- net VIBE-INDEX: now also Q4.G, R35.2; no longer R19.1
- net VIBE-MIDDLE: now also Q3.G, R34.2; no longer R18.1
- net VIBE-PALM: now also Q6.G, R37.2; no longer R21.1
- net VIBE-PINKY: now also Q1.G, R32.2; no longer R16.1
- net VIBE-RING: now also Q2.G, R33.2; no longer R17.1
- net VIBE-THUMB: now also Q5.G, R36.2; no longer R20.1
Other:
- note removed: "ANALOG VOLTAGE AMPLIFIER"
- note removed: "ELECTROTACTILE ARRAYS"
- note removed: "ET ARRAY - INDEX"
- note removed: "ET ARRAY - MIDDLE"
- note removed: "ET ARRAY - PINKY"
- note removed: "ET ARRAY - RING"
- note removed: "ET ARRAY - THUMB"
- note removed: "SQW GENERATOR"
- note removed: "STAGE1"
- note removed: "STAGE2"
- note removed: "STAGE3"
- note removed: "TODO: CHECK VALUES (C1, POT1, R2,R3) AND VOLTAGE DIVIDER TO MAKE 1.8V"
- note removed: "TODO: Change I2C addr"
- note removed: "TODO: NAME ENABLE PIN"
- note removed: "Transfer: VBAT, SDA, SCL, GND"
- moved on the sheet: AVR_ISP, C1, C10, C11, C12, C13, C14, C15, C18, C2, C21, C22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

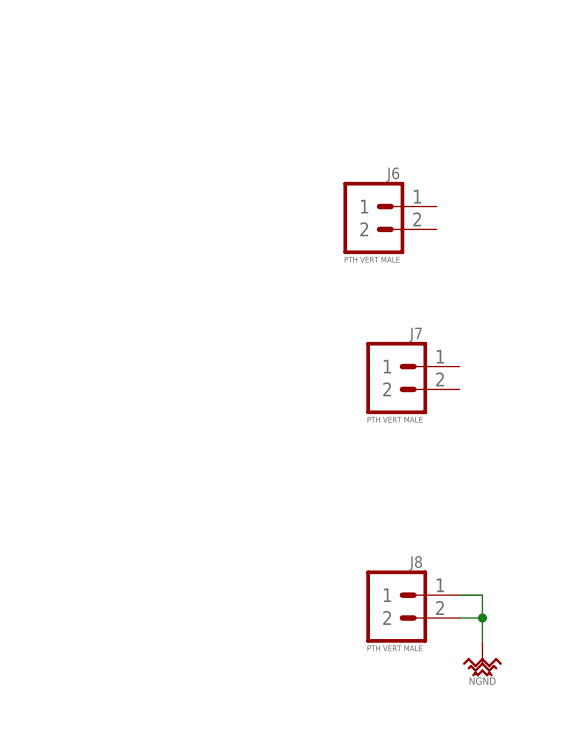
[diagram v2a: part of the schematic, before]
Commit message: Complete iteration of ET Extension and Touch Glove.  Verify PCA9685Servo library works and made appropriate changes in robotic arm master code.
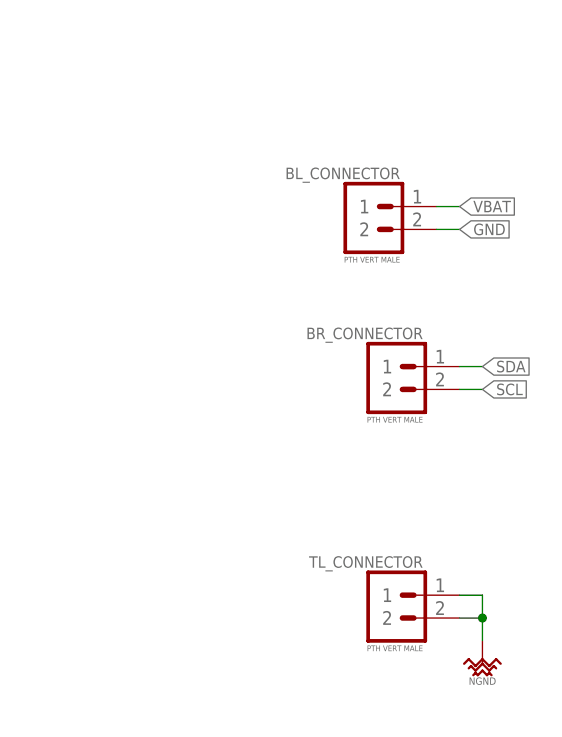
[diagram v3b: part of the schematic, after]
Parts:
- renumbered J6 to BL_CONNECTOR, J7 to BR_CONNECTOR, J8 to TL_CONNECTOR
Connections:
- net GND: now also BL_CONNECTOR.2
- net SCL: now also BR_CONNECTOR.2
- net SDA: now also BR_CONNECTOR.1
- net VBAT: now also BL_CONNECTOR.1
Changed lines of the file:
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@@
 <part name="SUPPLY83" library="_power_symbols" deviceset="VCC" device=""/>
 <part name="SUPPLY124" library="_power_symbols" deviceset="A1.8V" device=""/>
-<part name="J6" library="_connectors" deviceset="1X02" device="_PTH_VERT_MALE_2.54MM" package3d_urn="urn:adsk.eagle:package:4781708/8" value="PTH VERT MALE"/>
-<part name="J7" library="_connectors" deviceset="1X02" device="_PTH_VERT_MALE_2.54MM" package3d_urn="urn:adsk.eagle:package:4781708/8" value="PTH VERT MALE"/>
-<part name="J8" library="_connectors" deviceset="1X02" device="_PTH_VERT_MALE_2.54MM" package3d_urn="urn:adsk.eagle:package:4781708/8" value="PTH VERT MALE"/>
+<part name="BL_CONNECTOR" library="_connectors" deviceset="1X02" device="_PTH_VERT_MALE_2.54MM" package3d_urn="urn:adsk.eagle:package:4781708/8" value="PTH VERT MALE"/>
+<part name="BR_CONNECTOR" library="_connectors" deviceset="1X02" device="_PTH_VERT_MALE_2.54MM" package3d_urn="urn:adsk.eagle:package:4781708/8" value="PTH VERT MALE"/>
+<part name="TL_CONNECTOR" library="_connectors" deviceset="1X02" device="_PTH_VERT_MALE_2.54MM" package3d_urn="urn:adsk.eagle:package:4781708/8" value="PTH VERT MALE"/>
 <part name="J9" library="_connectors" deviceset="1X02" device="_PTH_VERT_MALE_2.54MM" package3d_urn="urn:adsk.eagle:package:4781708/8" value="PTH VERT MALE"/>
 <part name="SUPPLY51" library="_power_symbols" deviceset="NGND" device=""/>
@@
 <instance part="SUPPLY83" gate="VCC" x="299.72" y="449.58" smashed="yes"/>
 <instance part="SUPPLY124" gate="G$1" x="419.1" y="132.08" smashed="yes"/>
-<instance part="J6" gate="G$1" x="650.24" y="505.46" smashed="yes">
+<instance part="BL_CONNECTOR" gate="G$1" x="650.24" y="505.46" smashed="yes">
 <attribute name="VALUE" x="653.796" y="499.872" size="0.635" layer="96" font="vector" ratio="10" align="top-right"/>
 <attribute name="NAME" x="653.796" y="508.508" size="1.27" layer="95" font="vector" ratio="10" align="bottom-right"/>
 </instance>
-<instance part="J7" gate="G$1" x="652.78" y="487.68" smashed="yes">
+<instance part="BR_CONNECTOR" gate="G$1" x="652.78" y="487.68" smashed="yes">
 <attribute name="VALUE" x="656.336" y="482.092" size="0.635" layer="96" font="vector" ratio="10" align="top-right"/>
 <attribute name="NAME" x="656.336" y="490.728" size="1.27" layer="95" font="vector" ratio="10" align="bottom-right"/>
 </instance>
-<instance part="J8" gate="G$1" x="652.78" y="462.28" smashed="yes">
+<instance part="TL_CONNECTOR" gate="G$1" x="652.78" y="462.28" smashed="yes">
 <attribute name="VALUE" x="656.336" y="456.692" size="0.635" layer="96" font="vector" ratio="10" align="top-right"/>
 <attribute name="NAME" x="656.336" y="465.328" size="1.27" layer="95" font="vector" ratio="10" align="bottom-right"/>
@@
 <pinref part="GND1" gate="GND" pin="GND"/>
 </segment>
+<segment>
+<pinref part="BL_CONNECTOR" gate="G$1" pin="2"/>
+<wire x1="660.4" y1="502.92" x2="657.86" y2="502.92" width="0.1524" layer="91"/>
+<label x="660.4" y="502.92" size="1.27" layer="95" font="vector" ratio="10" xref="yes"/>
+</segment>
 </net>
 <net name="VCC" class="1">
@@
 <wire x1="381" y1="401.32" x2="381" y2="406.4" width="0.1524" layer="91"/>
 </segment>
+<segment>
+<pinref part="BR_CONNECTOR" gate="G$1" pin="1"/>
+<wire x1="662.94" y1="487.68" x2="660.4" y2="487.68" width="0.1524" layer="91"/>
+<label x="662.94" y="487.68" size="1.27" layer="95" font="vector" ratio="10" xref="yes"/>
+</segment>
 </net>
 <net name="SCL" class="0">
@@
 <wire x1="375.92" y1="406.4" x2="375.92" y2="403.86" width="0.1524" layer="91"/>
 <junction x="375.92" y="403.86"/>
+</segment>
+<segment>
+<pinref part="BR_CONNECTOR" gate="G$1" pin="2"/>
+<wire x1="662.94" y1="485.14" x2="660.4" y2="485.14" width="0.1524" layer="91"/>
+<label x="662.94" y="485.14" size="1.27" layer="95" font="vector" ratio="10" xref="yes"/>
 </segment>
 </net>
@@
 </segment>
 <segment>
-<pinref part="J8" gate="G$1" pin="1"/>
+<pinref part="TL_CONNECTOR" gate="G$1" pin="1"/>
 <wire x1="660.4" y1="462.28" x2="662.94" y2="462.28" width="0.1524" layer="91"/>
 <wire x1="662.94" y1="462.28" x2="662.94" y2="459.74" width="0.1524" layer="91"/>
-<pinref part="J8" gate="G$1" pin="2"/>
+<pinref part="TL_CONNECTOR" gate="G$1" pin="2"/>
 <wire x1="662.94" y1="459.74" x2="662.94" y2="457.2" width="0.1524" layer="91"/>
 <wire x1="660.4" y1="459.74" x2="662.94" y2="459.74" width="0.1524" layer="91"/>
@@
 <pinref part="SUPPLY15" gate="G$1" pin="VBAT"/>
 </segment>
-</net>
+<segment>
+<pinref part="BL_CONNECTOR" gate="G$1" pin="1"/>
+<wire x1="660.4" y1="505.46" x2="657.86" y2="505.46" width="0.1524" layer="91"/>
+<label x="660.4" y="505.46" size="1.27" layer="95" font="vector" ratio="10" xref="yes"/>
+</segment>
+</net>

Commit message: Fix sizing of some text on board.  Clean up schematic.
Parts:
- removed FLEX-INDEX2, FLEX-MIDDLE2, FLEX-PINKY2, FLEX-RING2, FLEX-THUMB2: 10K, _sensors:FLEX_SENSOR_0530470210_VERT-MALE_PITCH-1.25MM
- added FLEX-INDEX, FLEX-MIDDLE, FLEX-PINKY, FLEX-RING, FLEX-THUMB: 10K, _sensors:FLEX_SENSOR_0530470210_VERT-MALE_PITCH-1.25MM
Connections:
- net FLEX-INDEX2 renamed FLEX-INDEX
- net FLEX-MIDDLE2 renamed FLEX-MIDDLE
- net FLEX-PINKY2 renamed FLEX-PINKY
- net FLEX-RING2 renamed FLEX-RING
- net FLEX-THUMB2 renamed FLEX-THUMB
- net N$10001: now also FLEX-PINKY.-; no longer FLEX-PINKY2.-
- net N$1004: now also FLEX-THUMB.-; no longer FLEX-THUMB2.-
- net N$38: now also FLEX-INDEX.-; no longer FLEX-INDEX2.-
- net N$41: now also FLEX-RING.-; no longer FLEX-RING2.-
- net N$991: now also FLEX-MIDDLE.-; no longer FLEX-MIDDLE2.-
- net VSENSOR: now also FLEX-INDEX.+, FLEX-MIDDLE.+, FLEX-PINKY.+, FLEX-RING.+, FLEX-THUMB.+; no longer FLEX-INDEX2.+, FLEX-MIDDLE2.+, FLEX-PINKY2.+, FLEX-RING2.+, FLEX-THUMB2.+
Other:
- moved on the sheet: AVR_ISP, BL_CONNECTOR, BR_CONNECTOR, C22, C38, C44, C45, C46, C47, C48, DEMUX1, FTDI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

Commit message: Everything fucking works (have not tested ET driver extensively yet though)
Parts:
- C36: value 22pF/100V -> 22pF/100V/0402
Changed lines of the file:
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@@
 <part name="GND116" library="_power_symbols" deviceset="GND" device=""/>
 <part name="BALUN1" library="_radio_frequency" deviceset="BALUN" device="_SMD-0805_UNBAL/BAL-50/100" package3d_urn="urn:adsk.eagle:package:2933573/1" value="50/100"/>
-<part name="C36" library="_capacitors" deviceset="22PF" device="_CER_SMD-0402-100V-5%" package3d_urn="urn:adsk.eagle:package:2886515/1" value="22pF/100V"/>
+<part name="C36" library="_capacitors" deviceset="22PF" device="_CER_SMD-0402-100V-5%" package3d_urn="urn:adsk.eagle:package:2886515/1" value="22pF/100V/0402"/>
 <part name="C35" library="_capacitors" deviceset="0.75PF" device="_CER_SMD-0402_50V-33%" package3d_urn="urn:adsk.eagle:package:2886515/1" value="0.75pF/50V"/>
 <part name="ANT" library="_radio_frequency" deviceset="ANTENNA" device="_SMD_CHP-2.45GHZ-0.5DBI-3W" package3d_urn="urn:adsk.eagle:package:2933495/1" value="2.45GHz"/>
